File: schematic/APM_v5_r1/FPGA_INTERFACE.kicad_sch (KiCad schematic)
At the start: 6 parts, among them J1 DF40C-60DS-0.4V(51), J15 FPGA FFC, J21 FPGA FMC, J3 DF40C-60DS-0.4V(51)

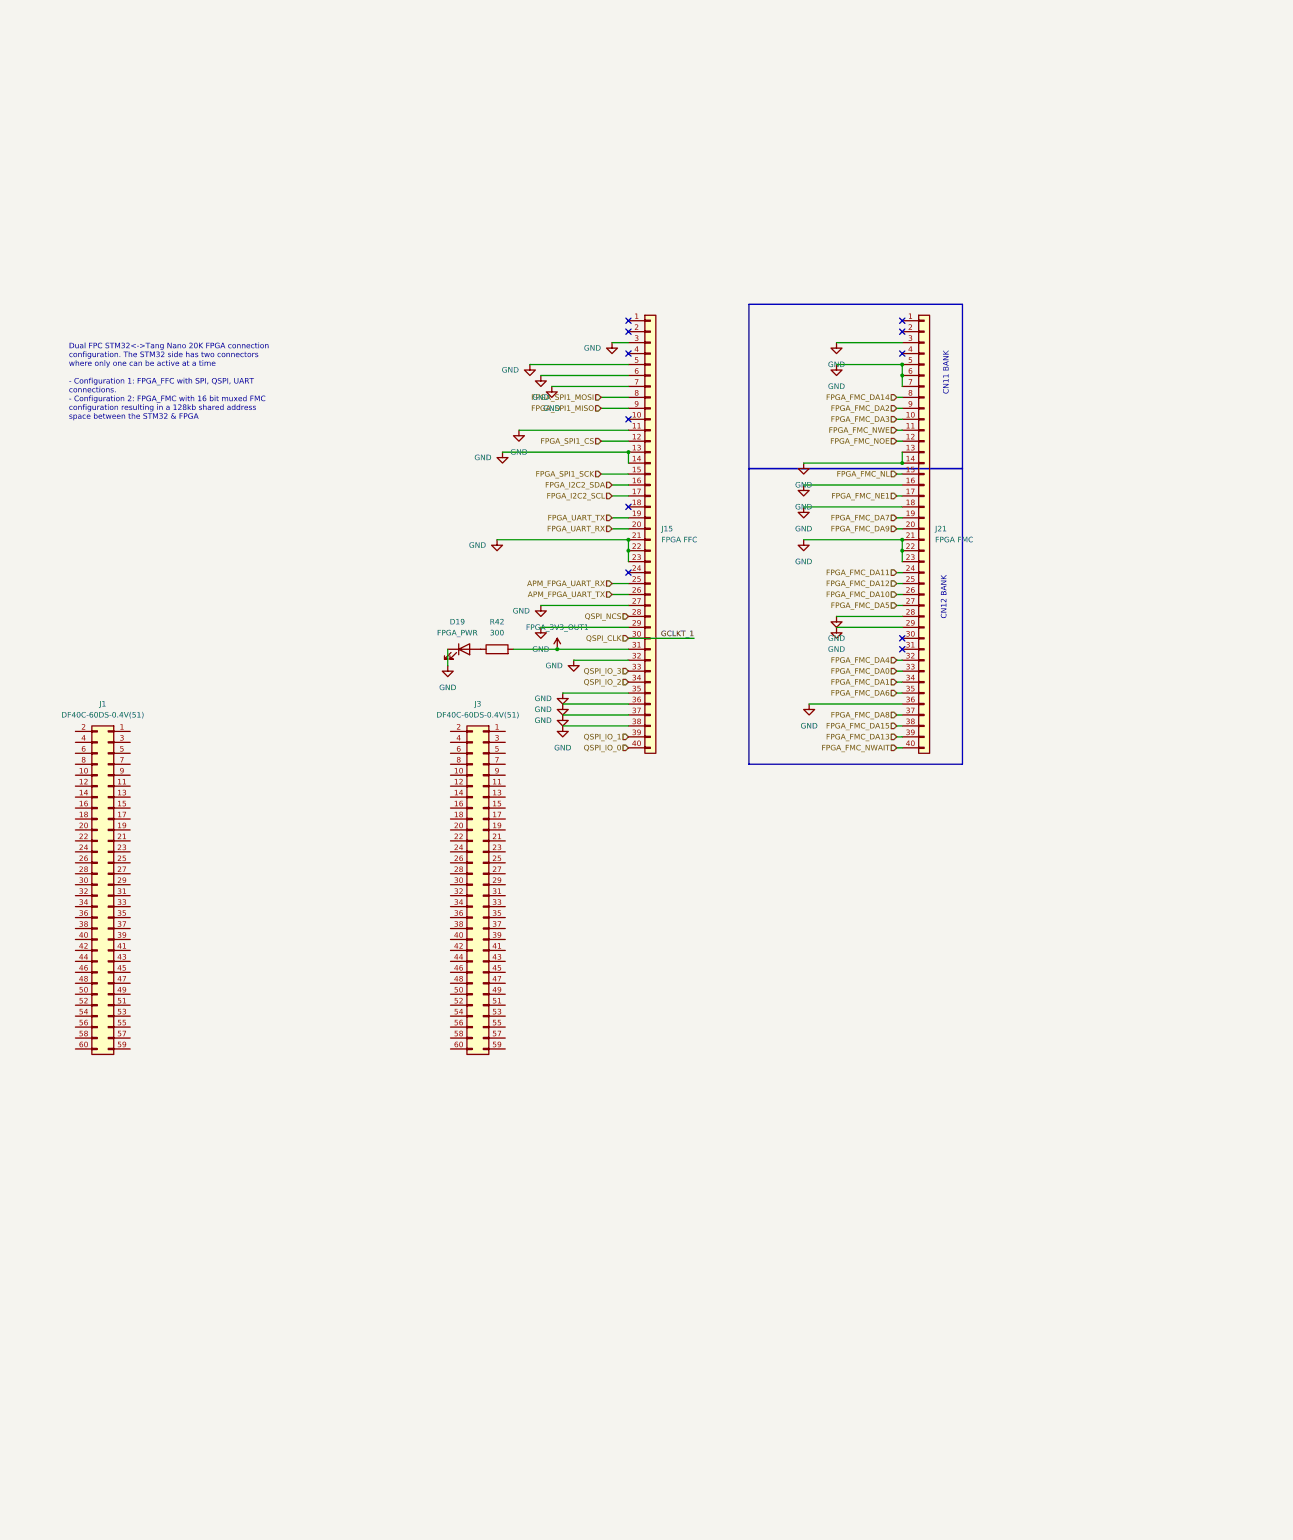
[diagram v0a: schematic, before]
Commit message: figuring out FFC traces next
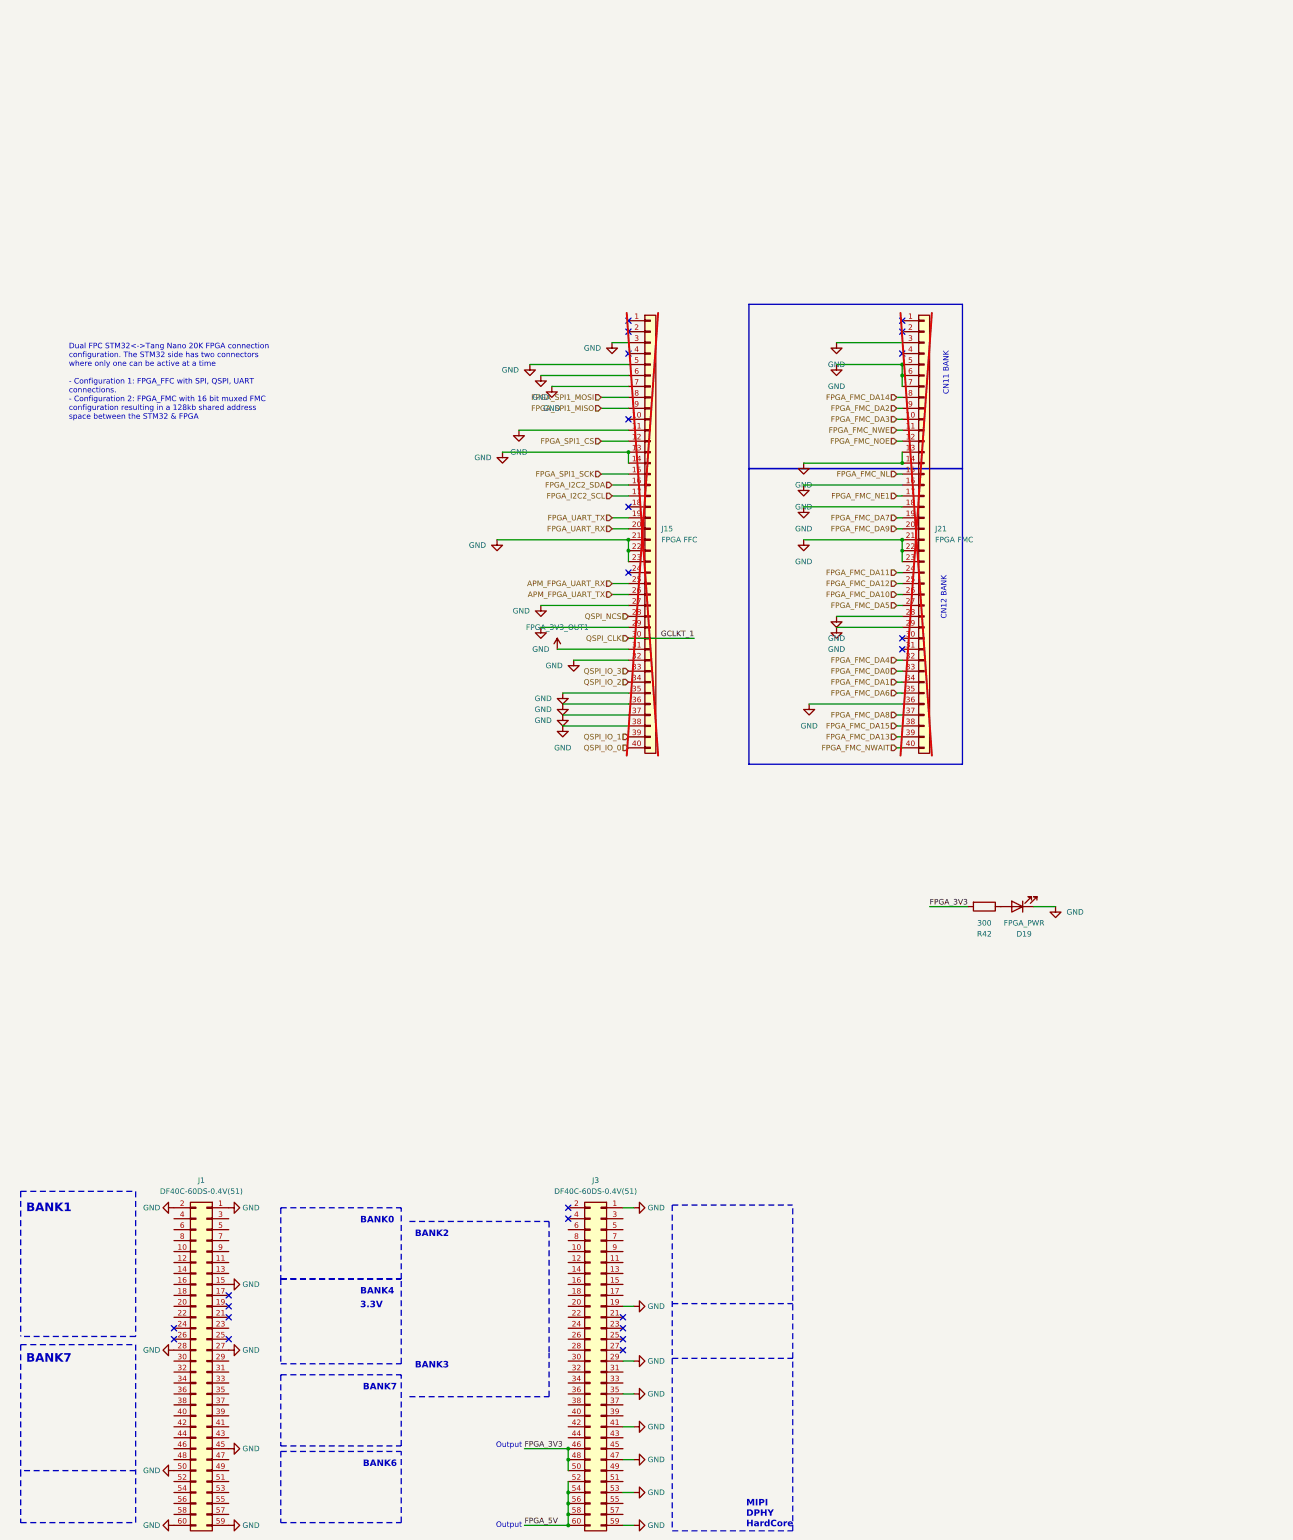
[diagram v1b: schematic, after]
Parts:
- J15, J21: now not fitted; now left out of the parts list
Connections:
- net FPGA_3V3_OUT1: no longer R42.2
- net GND: now also J1.1 (Pin_1), J1.15 (Pin_15), J1.2 (Pin_2), J1.27 (Pin_27), J1.28 (Pin_28), J1.45 (Pin_45), J1.50 (Pin_50), J1.59 (Pin_59), J1.60 (Pin_60), J3.1 (Pin_1), J3.19 (Pin_19), J3.29 (Pin_29), J3.35 (Pin_35), J3.41 (Pin_41), J3.47 (Pin_47), J3.53 (Pin_53), J3.59 (Pin_59)
- net FPGA_3V3: now reaches J3.46 (Pin_46)
- net FPGA_3V3: now also J3.48 (Pin_48), J3.50 (Pin_50), R42.2
- net FPGA_5V: now reaches J3.52 (Pin_52)
- net FPGA_5V: now also J3.54 (Pin_54), J3.56 (Pin_56), J3.58 (Pin_58), J3.60 (Pin_60)
- no-connect marks 11 -> 23
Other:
- note added: "3.3V"
- note added: "BANK0"
- note added: "BANK1"
- note added: "BANK2"
- note added: "BANK3"
- note added: "BANK4"
- note added: "BANK6"
- note added: "BANK7"
- note added: "MIPI DPHY HardCore"
- note added: "Output"
- moved on the sheet: D19, J1, J3, R42

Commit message: getting ACM and APM schematics put together. tool for FMC pin mapping verif
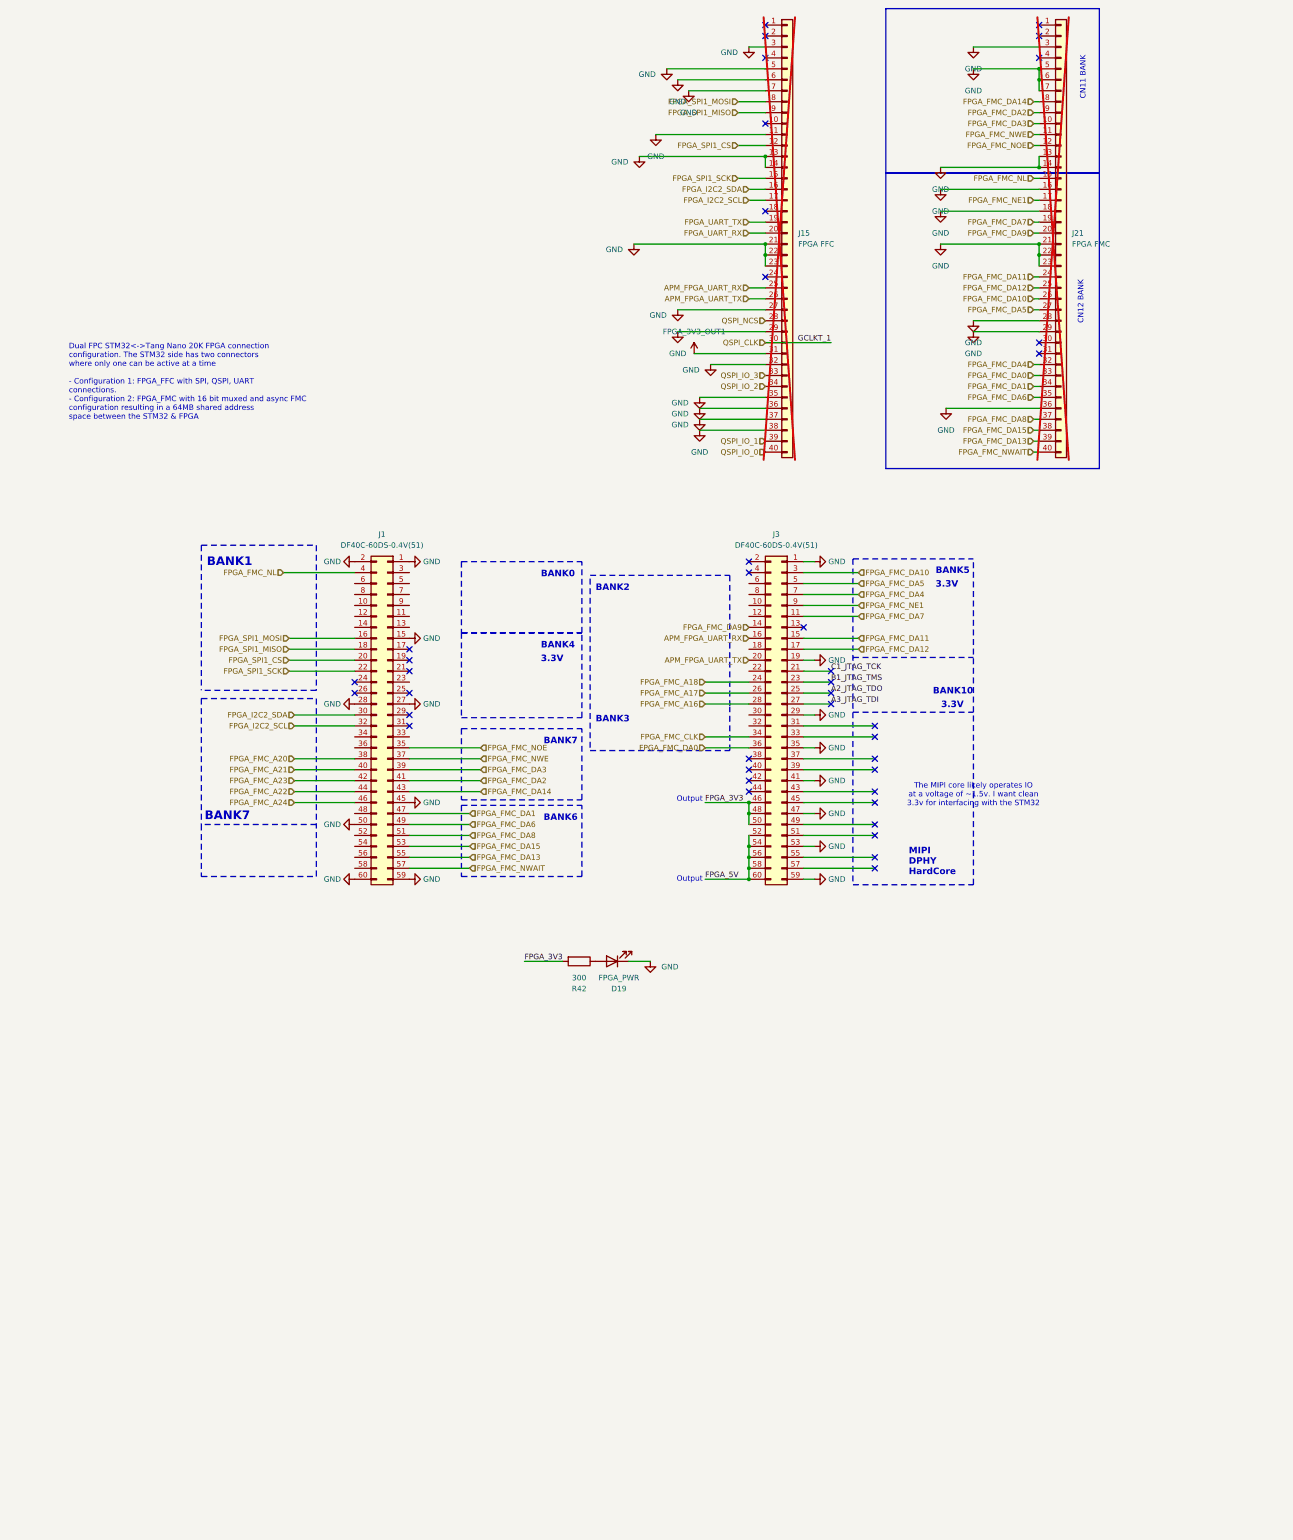
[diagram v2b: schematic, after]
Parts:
- J1, J3: footprint my_footprints:Hirose_DF40C-60DS-0.4V_2x30_P0.4mm -> my_footprints:HIROSE_DF40C-60DP-0.4V_51_
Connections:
- net APM_FPGA_UART_RX: now also J3.16 (Pin_16)
- net APM_FPGA_UART_TX: now also J3.20 (Pin_20)
- net FPGA_FMC_DA0: now also J3.36 (Pin_36)
- net FPGA_FMC_DA1: now also J1.47 (Pin_47)
- net FPGA_FMC_DA10: now also J3.3 (Pin_3)
- net FPGA_FMC_DA11: now also J3.15 (Pin_15)
- net FPGA_FMC_DA12: now also J3.17 (Pin_17)
- net FPGA_FMC_DA13: now also J1.55 (Pin_55)
- net FPGA_FMC_DA14: now also J1.43 (Pin_43)
- net FPGA_FMC_DA15: now also J1.53 (Pin_53)
- net FPGA_FMC_DA2: now also J1.41 (Pin_41)
- net FPGA_FMC_DA3: now also J1.39 (Pin_39)
- net FPGA_FMC_DA4: now also J3.7 (Pin_7)
- net FPGA_FMC_DA5: now also J3.5 (Pin_5)
- net FPGA_FMC_DA6: now also J1.49 (Pin_49)
- net FPGA_FMC_DA7: now also J3.11 (Pin_11)
- net FPGA_FMC_DA8: now also J1.51 (Pin_51)
- net FPGA_FMC_DA9: now also J3.14 (Pin_14)
- net FPGA_FMC_NE1: now also J3.9 (Pin_9)
- net FPGA_FMC_NL: now also J1.4 (Pin_4)
- net FPGA_FMC_NOE: now also J1.35 (Pin_35)
- net FPGA_FMC_NWAIT: now also J1.57 (Pin_57)
- net FPGA_FMC_NWE: now also J1.37 (Pin_37)
- net FPGA_I2C2_SCL: now also J1.32 (Pin_32)
- net FPGA_I2C2_SDA: now also J1.30 (Pin_30)
- net FPGA_SPI1_CS: now also J1.20 (Pin_20)
- net FPGA_SPI1_MISO: now also J1.18 (Pin_18)
- net FPGA_SPI1_MOSI: now also J1.16 (Pin_16)
- net FPGA_SPI1_SCK: now also J1.22 (Pin_22)
- net C1_JTAG_TCK: now reaches J3.21 (Pin_21)
- net B1_JTAG_TMS: now reaches J3.23 (Pin_23)
- net FPGA_FMC_A18: now reaches J3.24 (Pin_24)
- net A2_JTAG_TDO: now reaches J3.25 (Pin_25)
- net FPGA_FMC_A17: now reaches J3.26 (Pin_26)
- net A3_JTAG_TDI: now reaches J3.27 (Pin_27)
- net FPGA_FMC_A16: now reaches J3.28 (Pin_28)
- net FPGA_FMC_CLK: now reaches J3.34 (Pin_34)
- net FPGA_FMC_A20: now reaches J1.38 (Pin_38)
- net FPGA_FMC_A21: now reaches J1.40 (Pin_40)
- net FPGA_FMC_A23: now reaches J1.42 (Pin_42)
- net FPGA_FMC_A22: now reaches J1.44 (Pin_44)
- net FPGA_FMC_A24: now reaches J1.46 (Pin_46)
- no-connect marks 23 -> 40
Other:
- note added: "BANK10"
- note added: "BANK5"
- note added: "Dual FPC STM32<->Tang Nano 20K FPGA connection configuration. The STM32 side has two connectors where only one can be active at a time - Configuration 1: FPGA_FFC with SPI, QSPI, UART connections. - Configuration 2: FPGA_FMC with 16 bit muxed and async FMC configuration resulting in a 64MB shared address space between the STM32 & FPGA"
- note added: "The MIPI core likely operates IO at a voltage of ~1.5v. I want clean 3.3v for interfacing with the STM32"
- note removed: "Dual FPC STM32<->Tang Nano 20K FPGA connection configuration. The STM32 side has two connectors where only one can be active at a time - Configuration 1: FPGA_FFC with SPI, QSPI, UART connections. - Configuration 2: FPGA_FMC with 16 bit muxed FMC configuration resulting in a 128kb shared address space between the STM32 & FPGA"
- moved on the sheet: D19, J1, J15, J21, J3, R42

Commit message: adding renders and render script
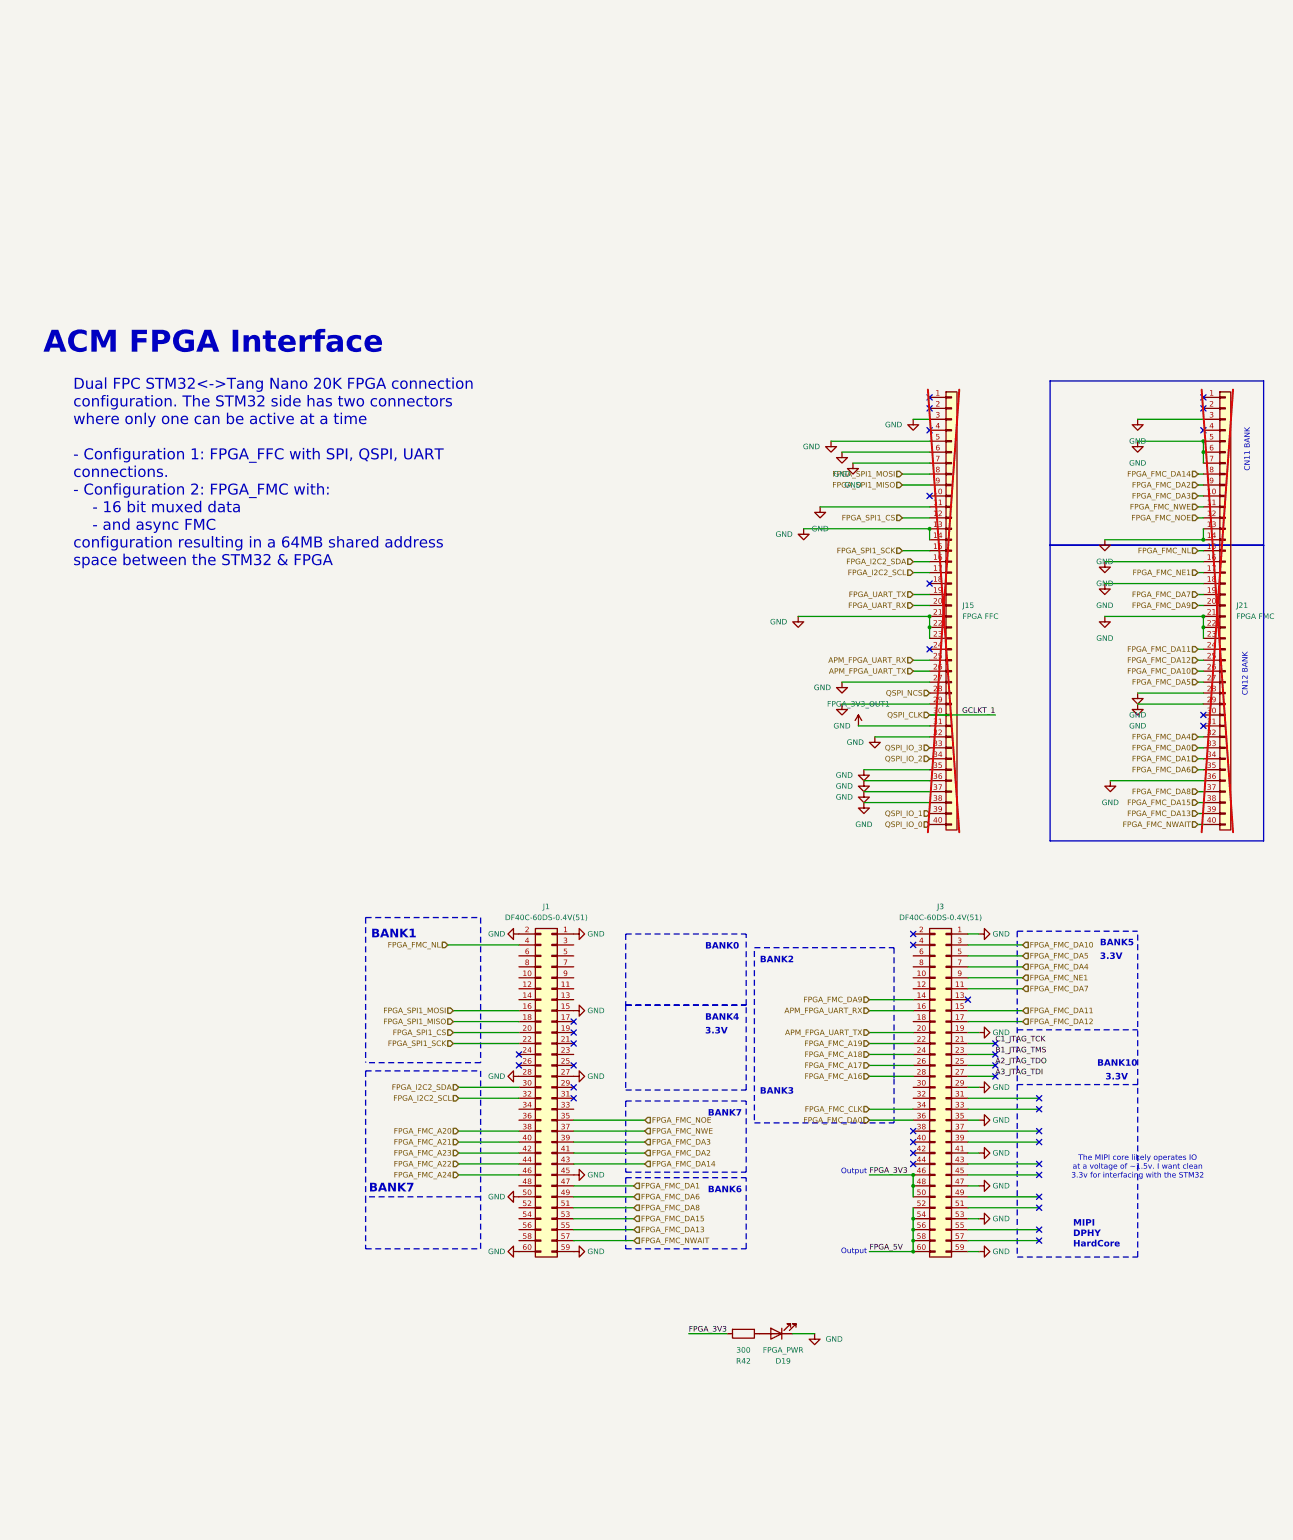
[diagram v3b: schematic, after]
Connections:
- net FPGA_FMC_A19: now reaches J3.22 (Pin_22)
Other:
- note added: "ACM FPGA Interface"
- note added: "Dual FPC STM32<->Tang Nano 20K FPGA connection configuration. The STM32 side has two connectors where only one can be active at a time - Configuration 1: FPGA_FFC with SPI, QSPI, UART connections. - Configuration 2: FPGA_FMC with: - 16 bit muxed data - and async FMC configuration resulting in a 64MB shared address space between the STM32 & FPGA"
- note removed: "Dual FPC STM32<->Tang Nano 20K FPGA connection configuration. The STM32 side has two connectors where only one can be active at a time - Configuration 1: FPGA_FFC with SPI, QSPI, UART connections. - Configuration 2: FPGA_FMC with 16 bit muxed and async FMC configuration resulting in a 64MB shared address space between the STM32 & FPGA"
- moved on the sheet: D19, J1, J15, J21, J3, R42
